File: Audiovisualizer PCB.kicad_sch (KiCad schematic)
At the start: 66 parts, among them J1 magnet, J10 Conn_01x02, J11 magnet, J12 magnet, J13 magnet, J14 Conn_01x02, J15 Conn_01x02, J16 Conn_01x02, J17 Conn_01x02, J18 Conn_01x02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

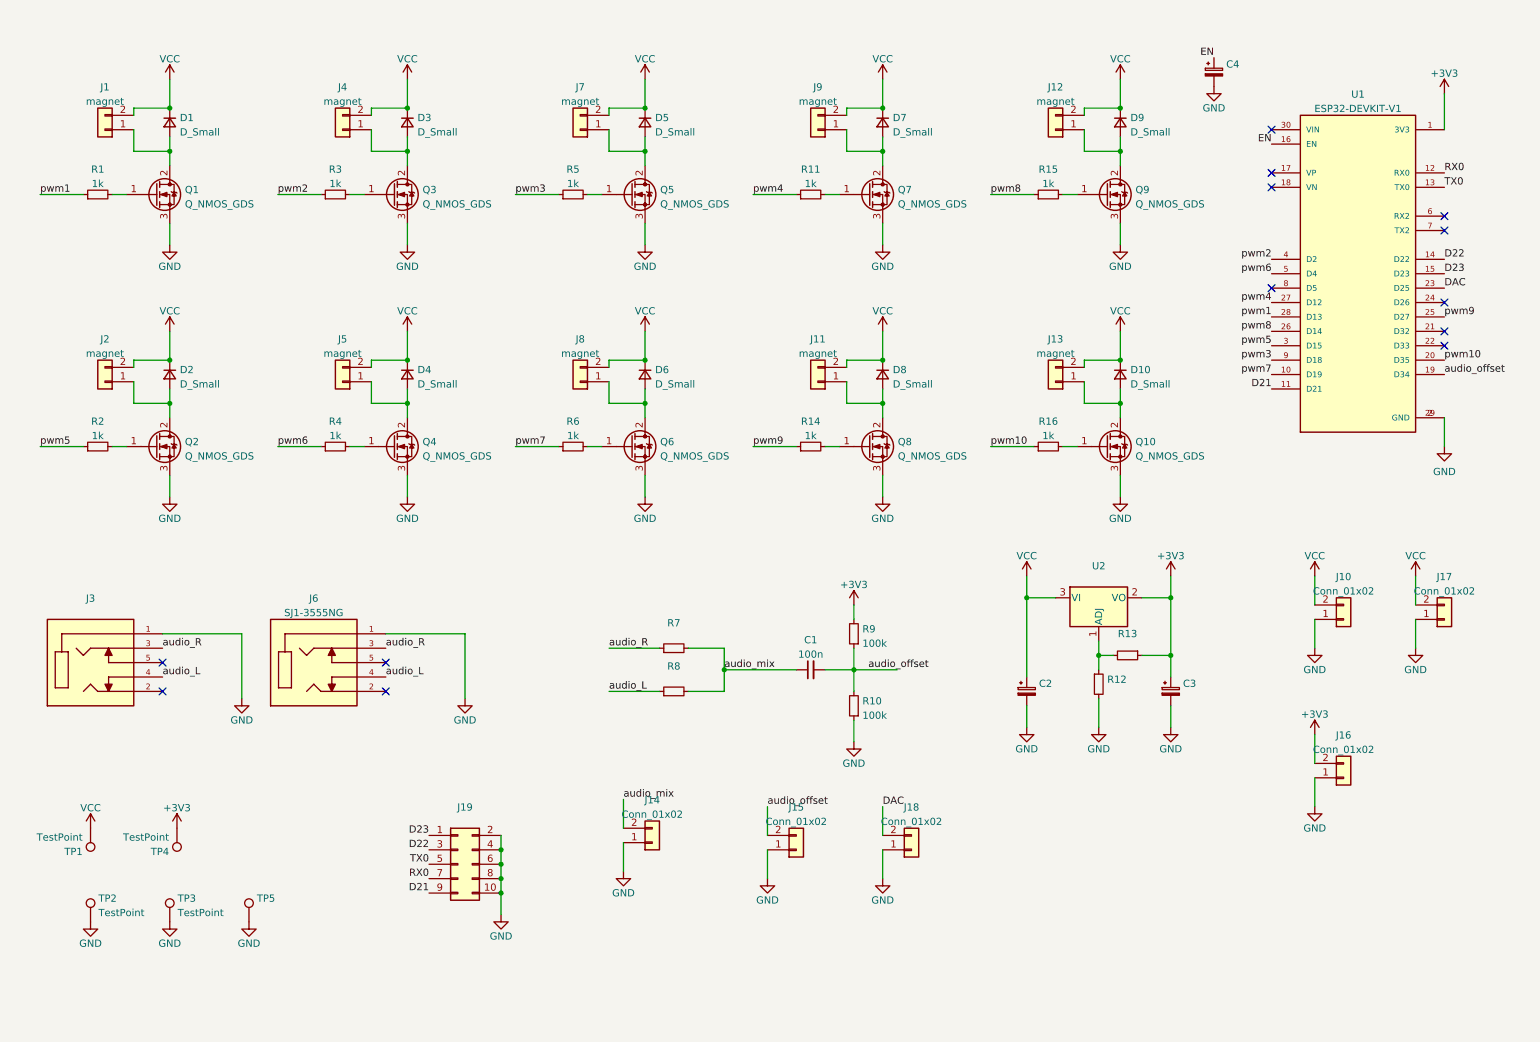
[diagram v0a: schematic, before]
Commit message: added component values
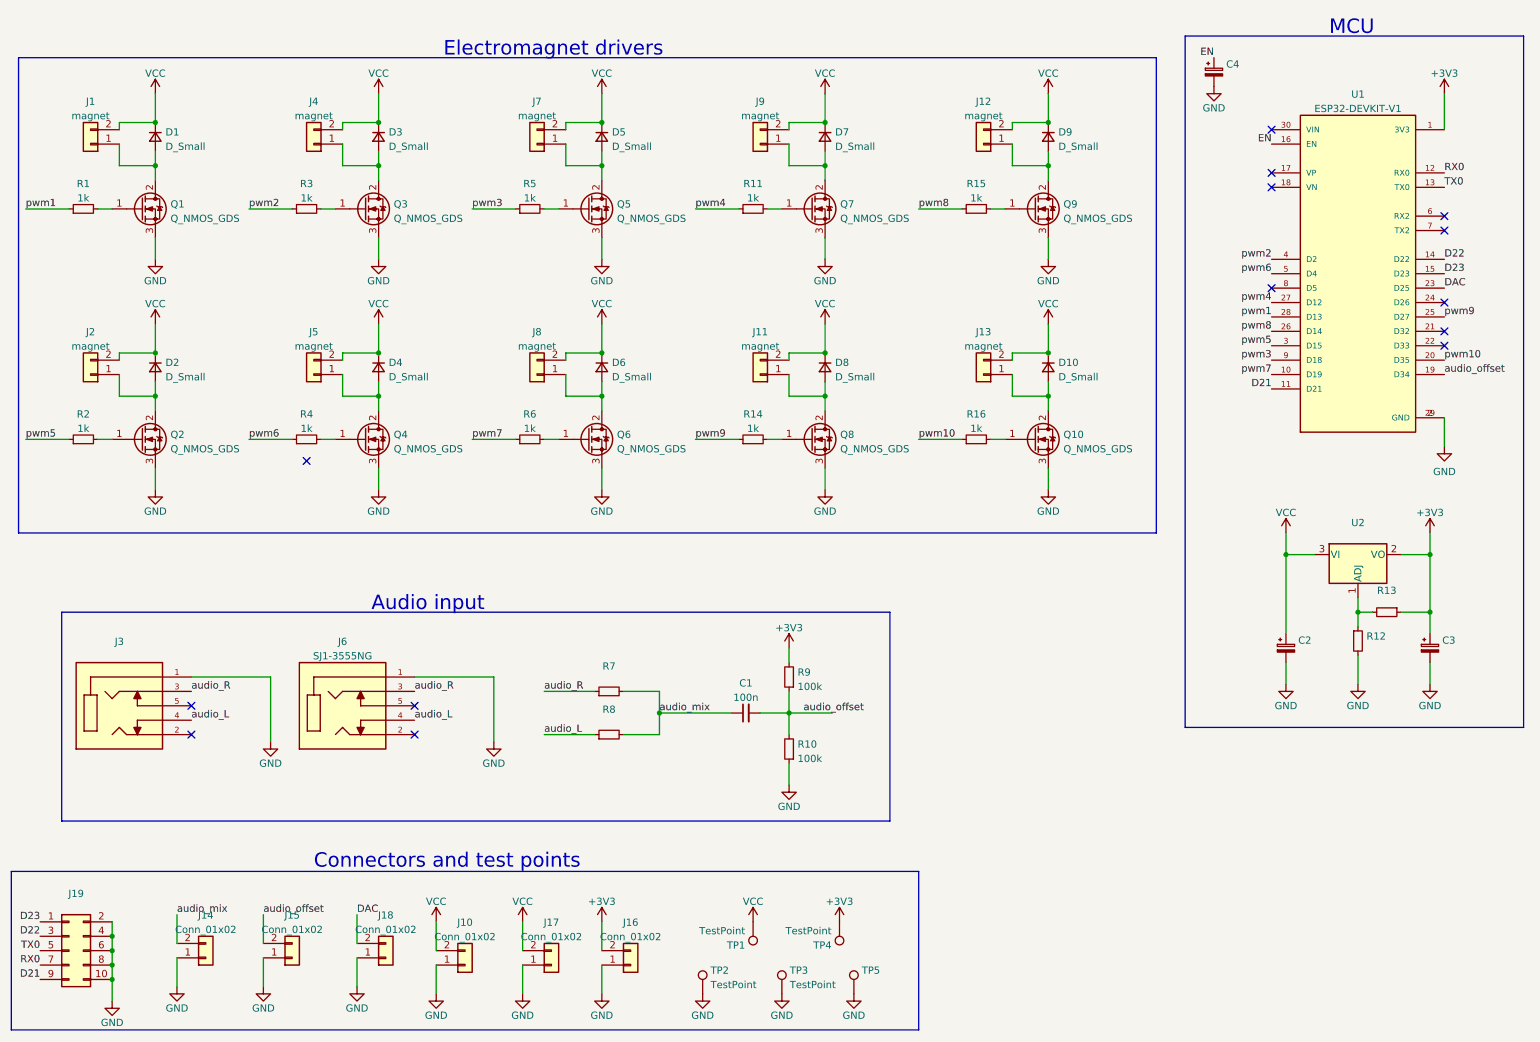
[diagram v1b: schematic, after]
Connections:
- no-connect marks 13 -> 14
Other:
- note added: "Audio input"
- note added: "Connectors and test points"
- note added: "Electromagnet drivers"
- note added: "MCU"
- moved on the sheet: C1, C2, C3, D1, D10, D2, D3, D4, D5, D6, D7, D8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

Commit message: updated pdf
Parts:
- D1, D10, D2, D3, D4, D5, D6, D7, D8, D9: value D_Small -> (none)
- Q1, Q10, Q2, Q3, Q4, Q5, Q6, Q7, Q8, Q9: value Q_NMOS_GDS -> (none)
